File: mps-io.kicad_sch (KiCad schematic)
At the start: 56 parts, among them J1 PMOD, J2 430451628, U1 SN74AC16PWR, U2 TLP2312, U3 TLP2312, U4 TLP2312, U5 TLP2312, U6 ILQ615-4X009T, U7 SN74AC14PWR

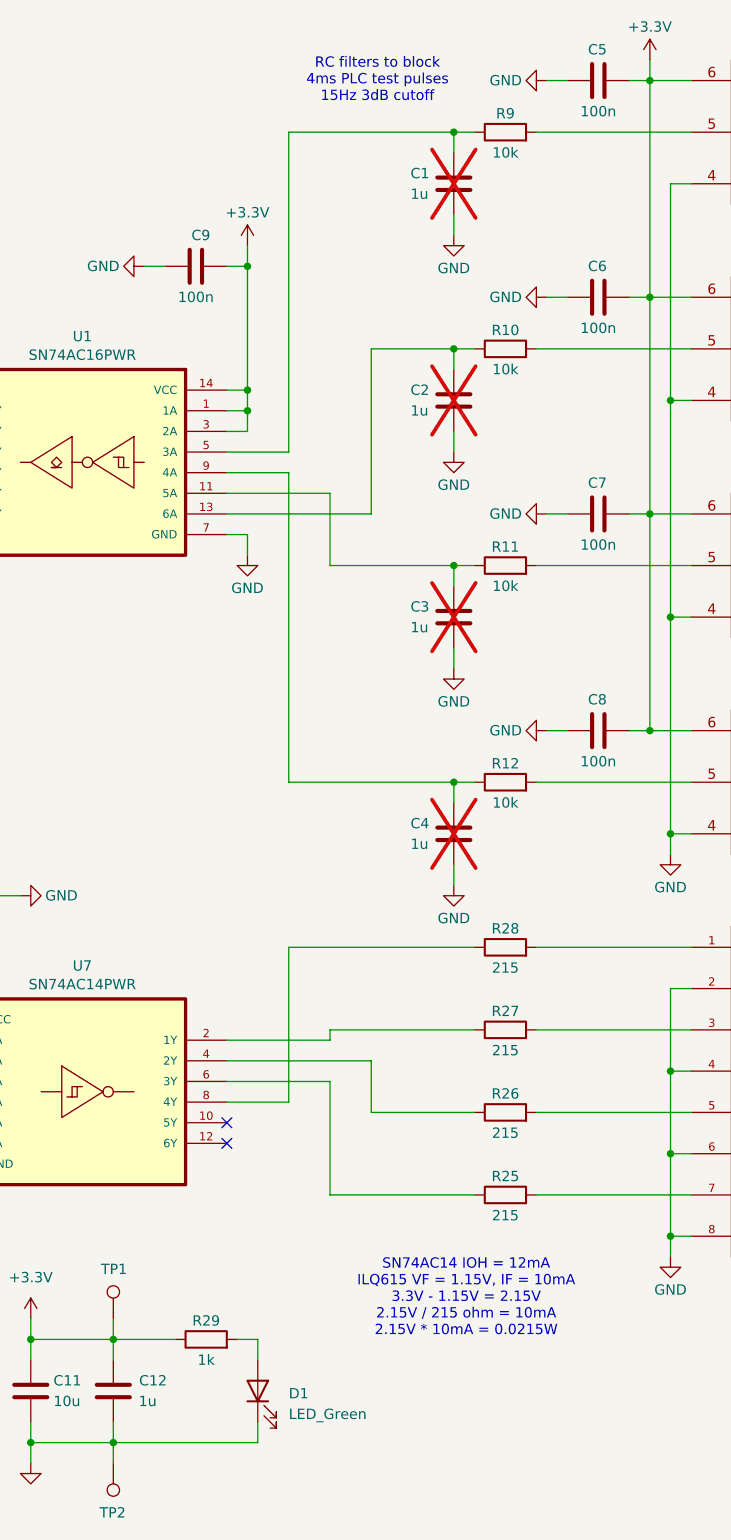
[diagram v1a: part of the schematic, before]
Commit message: Final tweaks: J2 pads, D1 603, no mask backoffs, table updates
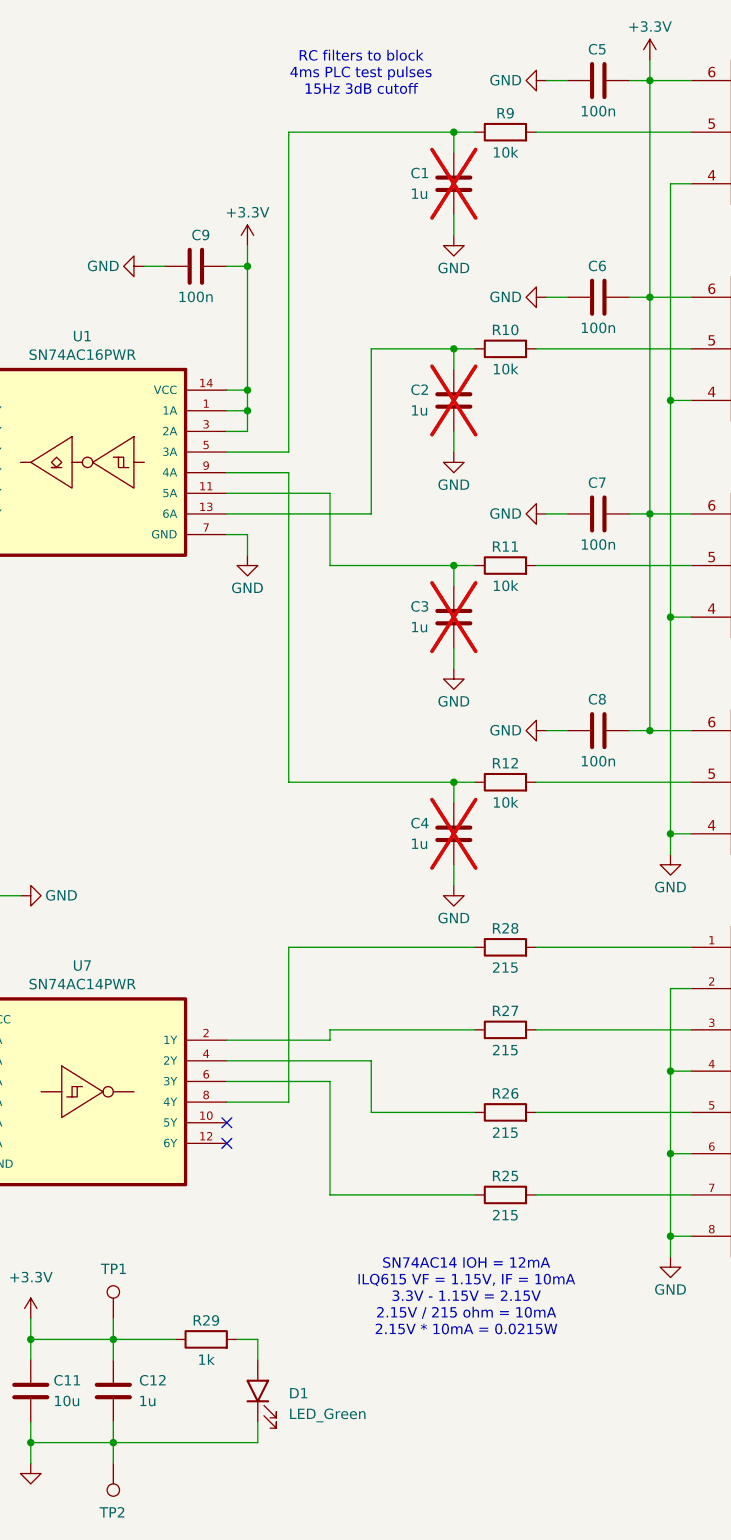
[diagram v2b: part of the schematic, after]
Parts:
- D1: footprint LED_SMD:LED_1206_3216Metric -> 0local:LED_0603_1608Metric

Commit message: re-add descriptions and datasheet
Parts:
- TP1, TP2: MANUFACTURER (none) -> Keystone Electronics
